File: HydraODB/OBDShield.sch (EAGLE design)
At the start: 31 parts, among them CN1 8p-2.54, J1 HYDRABUS_SHIELD_CON_HEADER_2X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, J2 HYDRABUS_SHIELD_CON_HEADER_2X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, J3 HYDRABUS_SHIELD_CON_HEADER_2X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, K1 TS-1188E, U1 SN65HVD233DG4, U2 SN65HVD233DG4, U3 CJ78M05-to252

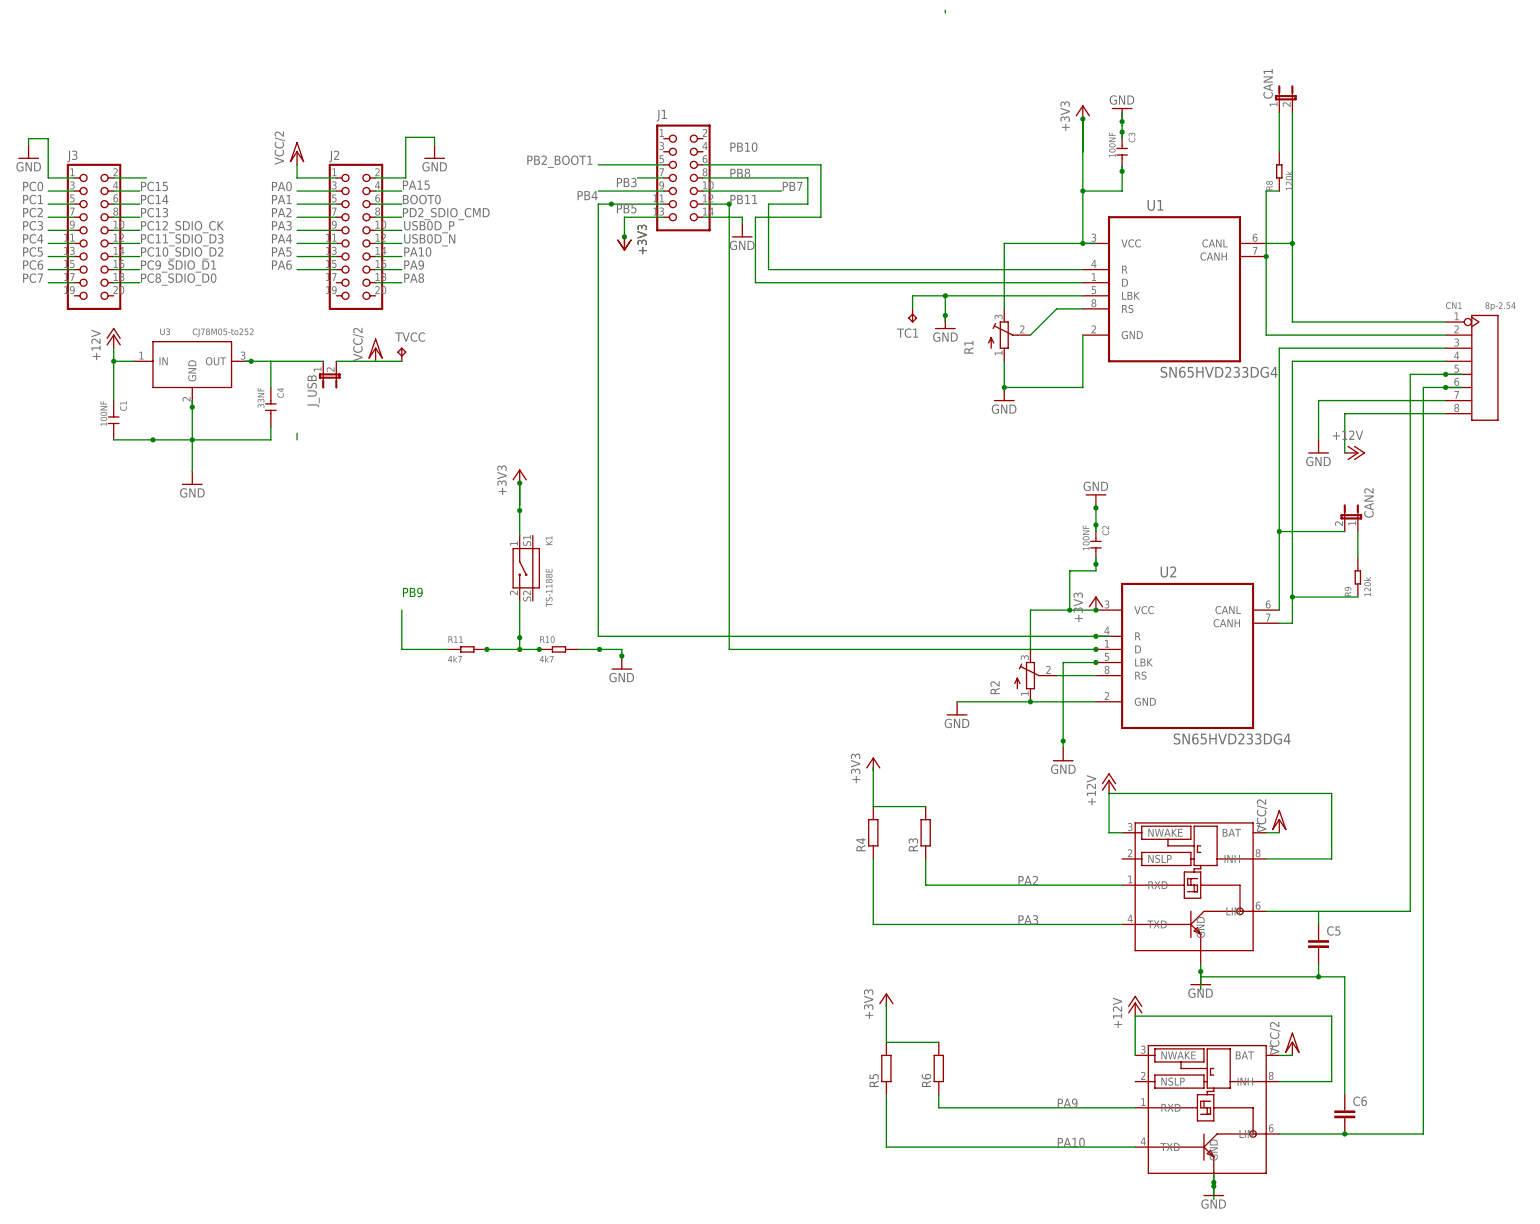
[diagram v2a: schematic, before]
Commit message: corrections on ground plate
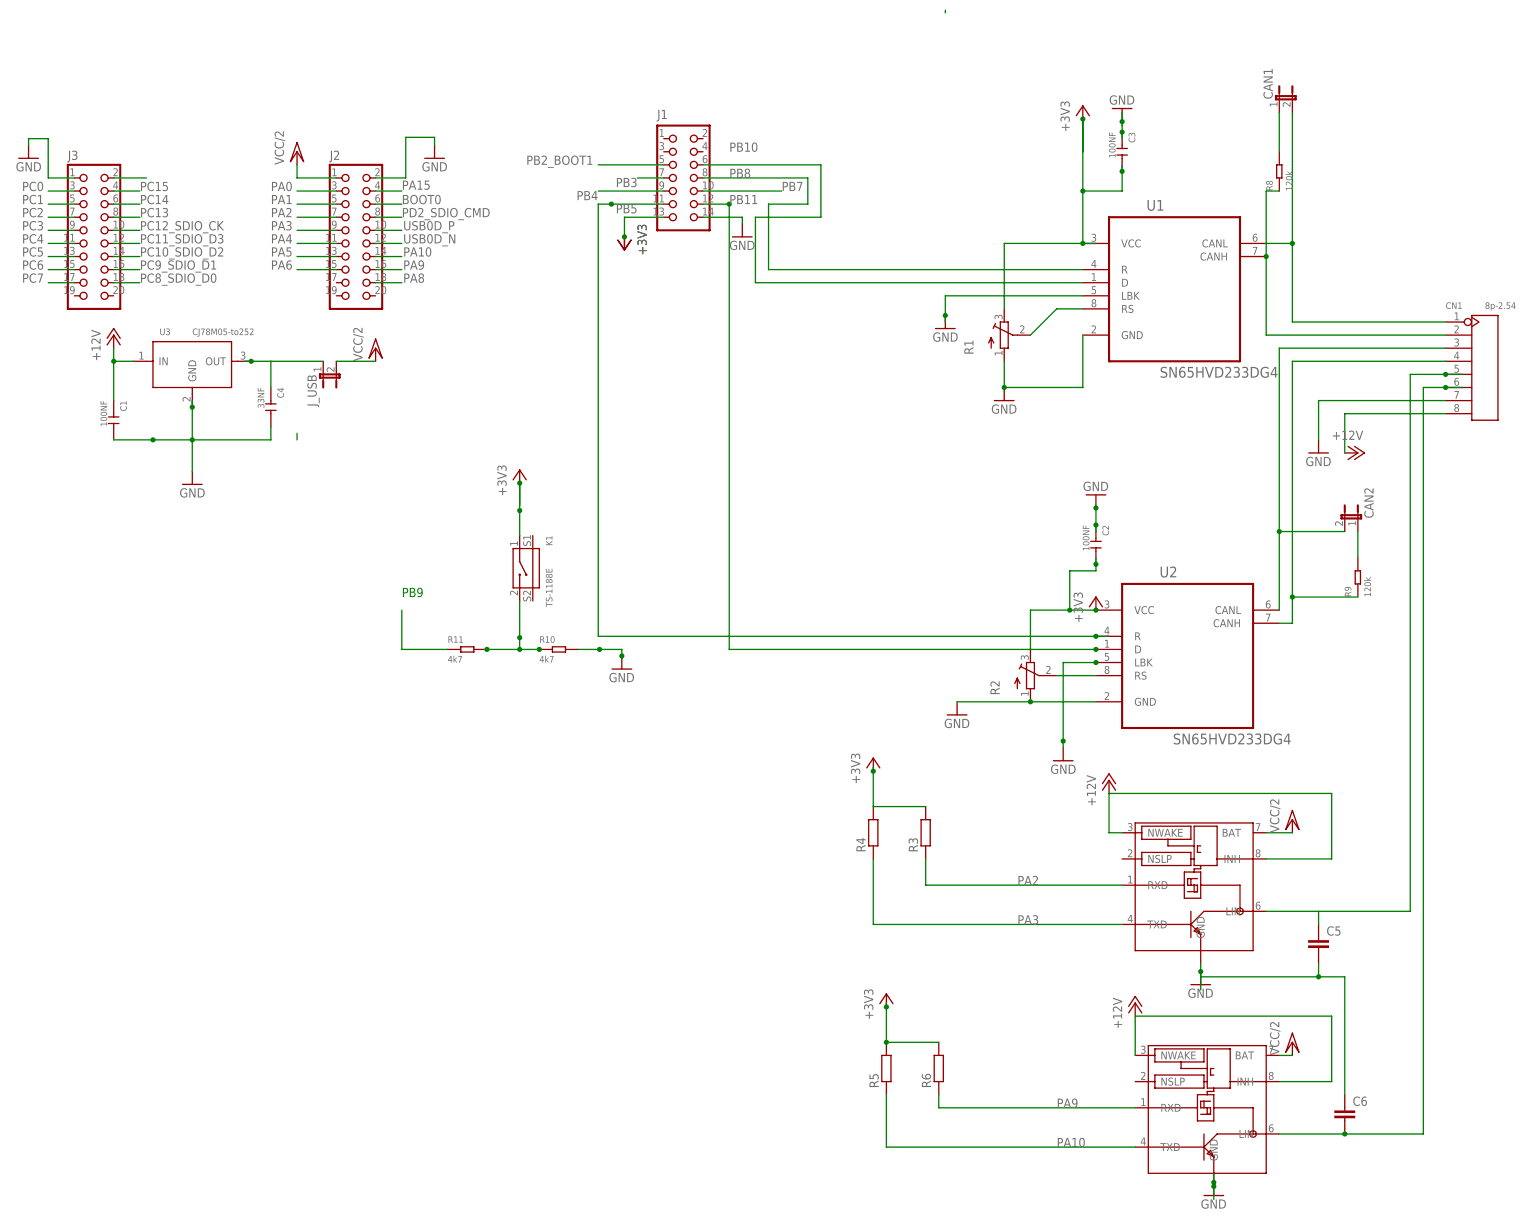
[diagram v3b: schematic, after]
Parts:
- removed TC1, TVCC: TPB2,54, testpad:TPB2,54
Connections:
- removed net N$13: R3.2, R4.2
- removed net N$18: R6.2
- net +3V3: now also R3.2, R4.2, R5.2, R6.2
- net GND: no longer TC1.TP
- net VCC/2: no longer TVCC.TP
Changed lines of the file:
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@@
 </class>
 <class number="2" name="VDD" width="0.3302" drill="0.3302">
-<clearance class="2" value="0.254"/>
+<clearance class="2" value="0.2032"/>
 </class>
 </classes>
@@
 <part name="U3" library="Seeed-OPL-ic" deviceset="PMIC-CJ78M05(TO-252)" device="" value="CJ78M05-to252"/>
 <part name="C4" library="Seeed-OPL-Capacitor" deviceset="CERAMIC-100NF-50V-20%-Y5V(0805)" device="" value="33NF"/>
-<part name="TVCC" library="testpad" deviceset="TP" device="B2,54"/>
-<part name="TC1" library="testpad" deviceset="TP" device="B2,54"/>
 <part name="CN1" library="Seeed-OPL-Connector" deviceset="DIP-BLACK-FEMALE-HEADER-VERT(8P-2.54)" device="" value="8p-2.54"/>
 <part name="U$1" library="nxp" deviceset="TJA1020" device="SO8"/>
@@
 <instance part="U3" gate="G$1" x="-15.24" y="91.44"/>
 <instance part="C4" gate="G$1" x="0" y="82.55" rot="R270"/>
-<instance part="TVCC" gate="G$1" x="25.4" y="93.98"/>
-<instance part="TC1" gate="G$1" x="124.46" y="99.06" rot="R180"/>
 <instance part="CN1" gate="G$1" x="235.458" y="90.17"/>
 <instance part="U$1" gate="G$1" x="172.72" y="-7.62"/>
@@
 <instance part="GND1" gate="1" x="180.34" y="-29.464"/>
 <instance part="GND4" gate="1" x="182.88" y="-70.358"/>
-<instance part="P+5" gate="G$1" x="195.58" y="2.54"/>
+<instance part="P+5" gate="G$1" x="198.12" y="2.54"/>
 <instance part="P+6" gate="G$1" x="198.12" y="-40.64"/>
 <instance part="P+8" gate="1" x="162.56" y="10.16"/>
@@
 <junction x="48.26" y="67.818"/>
 </segment>
+<segment>
+<pinref part="R4" gate="G$1" pin="2"/>
+<wire x1="116.84" y1="12.7" x2="116.84" y2="11.938" width="0.1524" layer="91"/>
+<pinref part="R3" gate="G$1" pin="2"/>
+<wire x1="116.84" y1="11.938" x2="116.84" y2="5.08" width="0.1524" layer="91"/>
+<wire x1="116.84" y1="5.08" x2="127" y2="5.08" width="0.1524" layer="91"/>
+<pinref part="+3V4" gate="G$1" pin="+3V3"/>
+<junction x="116.84" y="11.938"/>
+</segment>
+<segment>
+<pinref part="R6" gate="G$1" pin="2"/>
+<wire x1="119.38" y1="-33.02" x2="119.38" y2="-33.782" width="0.1524" layer="91"/>
+<wire x1="119.38" y1="-33.782" x2="119.38" y2="-40.64" width="0.1524" layer="91"/>
+<wire x1="119.38" y1="-40.64" x2="129.54" y2="-40.64" width="0.1524" layer="91"/>
+<pinref part="R5" gate="G$1" pin="2"/>
+<junction x="119.38" y="-40.64"/>
+<pinref part="+3V7" gate="G$1" pin="+3V3"/>
+<junction x="119.38" y="-33.782"/>
+</segment>
 </net>
 <net name="GND" class="2">
@@
 <wire x1="130.81" y1="100.33" x2="130.81" y2="99.06" width="0.1524" layer="91"/>
 <junction x="130.81" y="100.33"/>
-<pinref part="TC1" gate="G$1" pin="TP"/>
-<wire x1="124.46" y1="101.6" x2="124.46" y2="104.14" width="0.1524" layer="91"/>
-<wire x1="124.46" y1="104.14" x2="130.81" y2="104.14" width="0.1524" layer="91"/>
-<junction x="130.81" y="104.14"/>
 </segment>
 <segment>
@@
 <wire x1="12.7" y1="91.44" x2="20.32" y2="91.44" width="0.1524" layer="91"/>
 <pinref part="P+4" gate="G$1" pin="VCC/2"/>
-<pinref part="TVCC" gate="G$1" pin="TP"/>
-<wire x1="20.32" y1="91.44" x2="25.4" y2="91.44" width="0.1524" layer="91"/>
 </segment>
 <segment>
 <pinref part="U$1" gate="G$1" pin="BAT"/>
 <pinref part="P+5" gate="G$1" pin="VCC/2"/>
-<wire x1="193.04" y1="0" x2="195.58" y2="0" width="0.1524" layer="91"/>
+<wire x1="193.04" y1="0" x2="198.12" y2="0" width="0.1524" layer="91"/>
 </segment>
 <segment>
@@
 </segment>
 </net>
-<net name="N$13" class="0">
-<segment>
-<pinref part="R4" gate="G$1" pin="2"/>
-<wire x1="116.84" y1="12.7" x2="116.84" y2="5.08" width="0.1524" layer="91"/>
-<pinref part="R3" gate="G$1" pin="2"/>
-<wire x1="116.84" y1="5.08" x2="127" y2="5.08" width="0.1524" layer="91"/>
-</segment>
-</net>
-<net name="N$18" class="0">
-<segment>
-<pinref part="R6" gate="G$1" pin="2"/>
-<wire x1="119.38" y1="-33.02" x2="119.38" y2="-40.64" width="0.1524" layer="91"/>
-<wire x1="119.38" y1="-40.64" x2="129.54" y2="-40.64" width="0.1524" layer="91"/>
-</segment>
-</net>
